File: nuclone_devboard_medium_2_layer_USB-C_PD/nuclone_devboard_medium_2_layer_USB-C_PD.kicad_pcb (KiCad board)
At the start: 2 copper layers, 50 x 76.2 mm, 40 parts, among them J1 JTAG_2X05, J2 TYPE-C-31-M-12, J3 nuclone_medium_left, J4 nuclone_medium_right, J5 Conn_02x06_Odd_Even, SW1 RESET, SW2 Bootloader, U1 MCP1702-3.3V, U2 TPESD0504C6

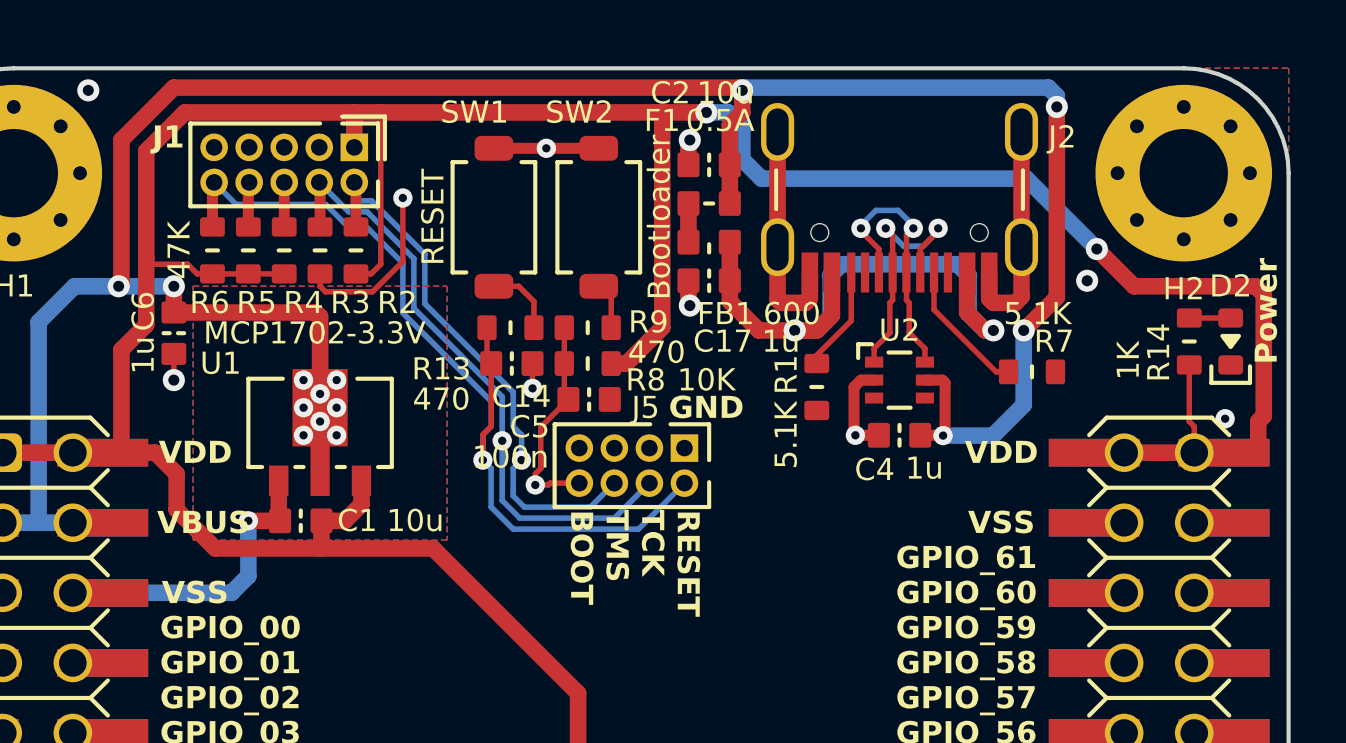
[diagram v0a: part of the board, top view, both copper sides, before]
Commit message: completed medium nuclone with USB-C PD connector
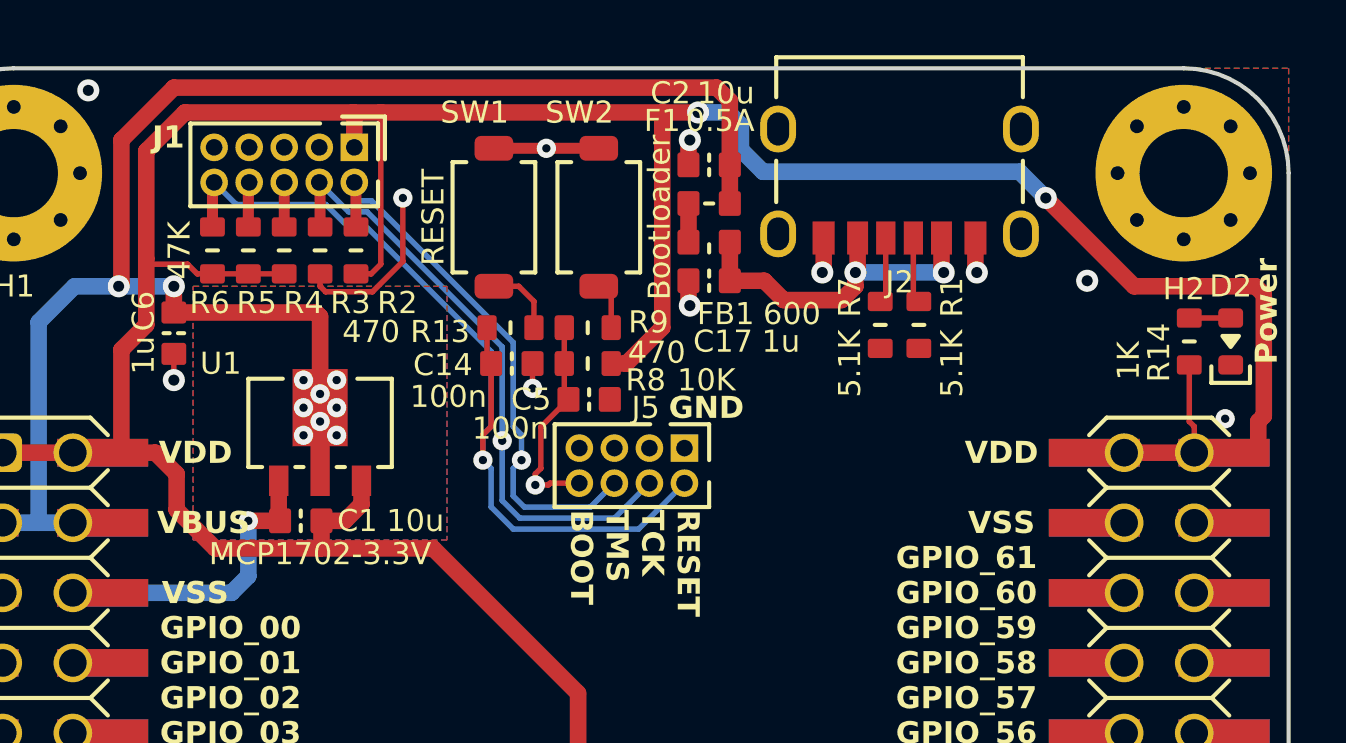
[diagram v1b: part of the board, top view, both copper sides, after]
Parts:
- removed C4: 1u, SquantorCapacitor:C_0603
- removed U2: TPESD0504C6, SquantorIC:SOT363-ONsemi
- J2: footprint SquantorUsb:USB-C-HRO-31-M-12_aisler -> SquantorUsb:USB-C-HRO-31-M-17_aisler
- N2: value V20240114 -> V20240124
- N5: value Nuclone Template V20240114 -> Nuclone Template V20240124
- moved R7 5.76 mm to (95.3, 70.3), turned to 90 degrees
- moved R1 4.33 mm to (96.7, 70.3)
- moved J2 1.25 mm to (96.0, 67.2)
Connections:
- C17 pad 2: Net-(C17-Pad2) -> /VUSB
- FB1 pad 2: Net-(C17-Pad2) -> /VUSB
- R1 pad 2: Net-(J2-CC2) -> Net-(J2-CC1)
- R7 pad 2: Net-(J2-CC1) -> Net-(J2-CC2)
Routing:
- net /VBUS: track 91.2 -> 60.2 mm, vias 14 -> 10
- net Net-(C17-Pad2): track 21.6 -> 0.00 mm, vias 2 -> 0
- net /VSS: track 44.6 -> 27.2 mm, vias 13 -> 14
- net /VUSB: track 0.00 -> 12.7 mm, vias 0 -> 2
- net /DP: track 10.4 -> 0.00 mm, vias 2 -> 0
- net /DN: track 9.60 -> 0.00 mm, vias 2 -> 0
- net Net-(J2-CC1): track 4.98 -> 2.38 mm
- net Net-(J2-CC2): track 3.89 -> 2.38 mm

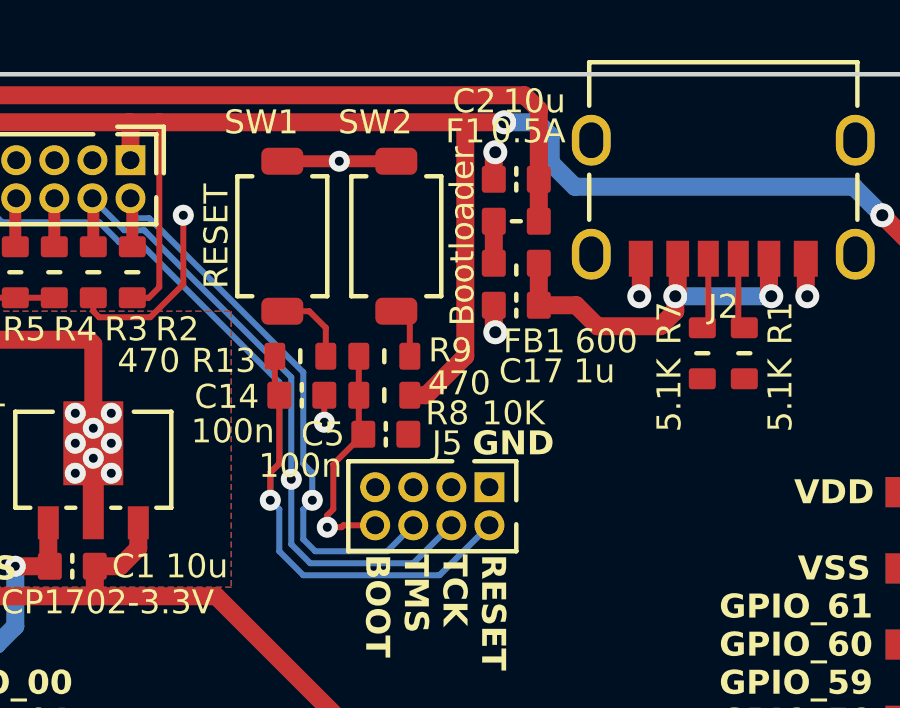
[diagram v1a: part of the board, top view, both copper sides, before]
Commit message: added diode in USB power line
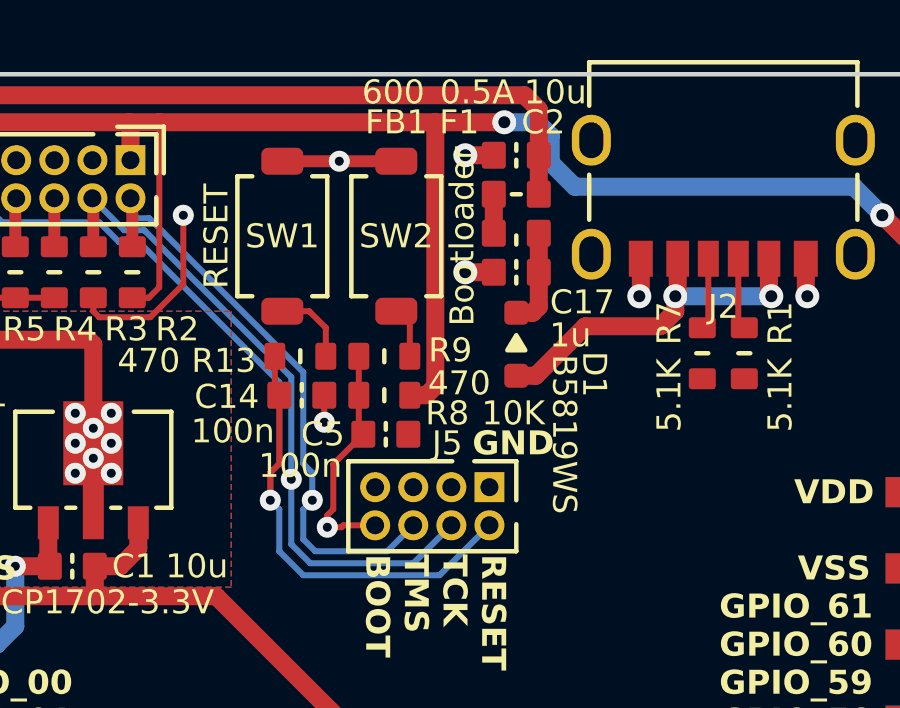
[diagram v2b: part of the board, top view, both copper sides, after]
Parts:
- added D1: B5819WS, SquantorDiodes:SOD-323-nexperia-hand, F.Cu at (89.1, 70.0)
- moved C17 1.10 mm to (89.1, 67.6)
- moved FB1 1.00 mm to (89.1, 66.3)
- moved F1 0.90 mm to (89.1, 65.0)
- moved C2 0.80 mm to (89.1, 63.7)
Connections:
- C17 pad 2: /VUSB -> Net-(D1-K)
- FB1 pad 2: /VUSB -> Net-(D1-K)
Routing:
- net Net-(D1-K): track 0.00 -> 3.28 mm
- net /VBUS: track 60.2 -> 59.3 mm

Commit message: small updates and positioning
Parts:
- moved N2 43.2 mm to (54.8, 103.0)
- moved N1 43.2 mm to (54.9, 99.0)
- moved N3 43.2 mm to (54.8, 104.6)
- moved N4 43.2 mm to (54.8, 104.8)
- moved R1 43.2 mm to (66.6, 39.3)
- moved R13 43.2 mm to (51.8, 39.4)
- moved R9 43.2 mm to (54.6, 39.4)
- moved C1 43.2 mm to (44.2, 46.4)
- moved C14 43.2 mm to (51.9, 40.7)
- moved C2 43.2 mm to (59.0, 32.7)
- moved C3 43.2 mm to (55.0, 60.0)
- moved C5 43.2 mm to (54.6, 42.0)
- moved D1 43.2 mm to (59.0, 39.0)
- moved D2 43.2 mm to (77.9, 39.9)
- moved F1 43.2 mm to (59.0, 34.0)
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
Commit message: updated boards
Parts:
- N2: value V20240124 -> V20240606
- N4: value NuClone Medium template V1.3 -> NuClone Medium template V1.5.1
- N5: value Nuclone Template V20240124 -> Nuclone Template V20240606
- moved C3 8.10 mm to (55.0, 68.1)
- moved C17 0.30 mm to (59.0, 36.9)
- moved D1 0.30 mm to (59.0, 39.3)
- moved H2 0.28 mm to (76.4, 33.6)
- moved H1 0.28 mm to (33.6, 33.6)
- moved H3 0.28 mm to (76.4, 102.6)
- moved H4 0.28 mm to (33.6, 102.6)
- moved FB1 0.20 mm to (59.0, 35.5)
- moved J5 0.20 mm to (56.2, 44.6)
- moved F1 0.10 mm to (59.0, 34.1)
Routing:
- net /VDD: track 128.1 -> 136.2 mm
- net /VSS: track 27.2 -> 34.8 mm
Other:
- outline, holes or cut-outs redrawn

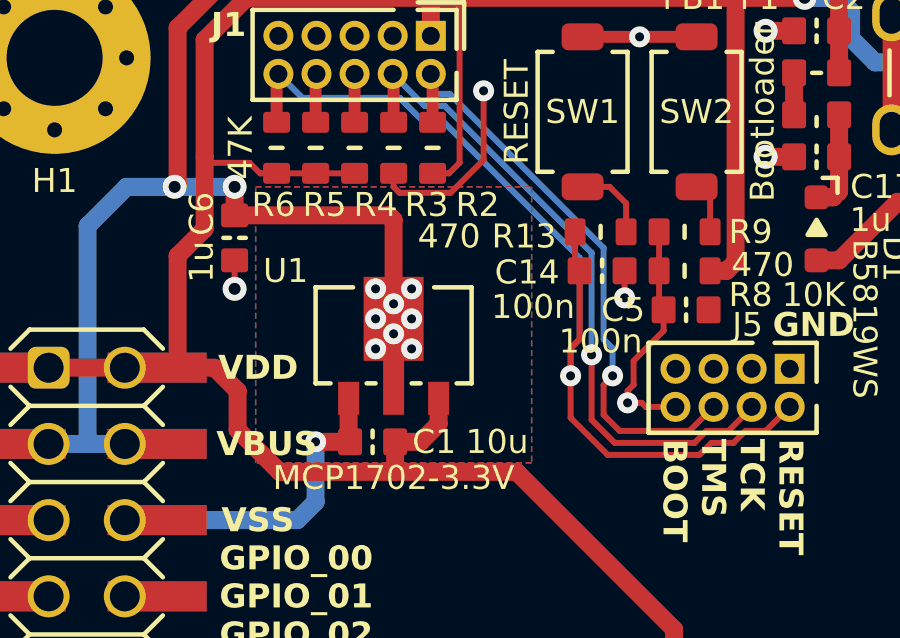
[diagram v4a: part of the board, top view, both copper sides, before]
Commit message: updated silkscreen
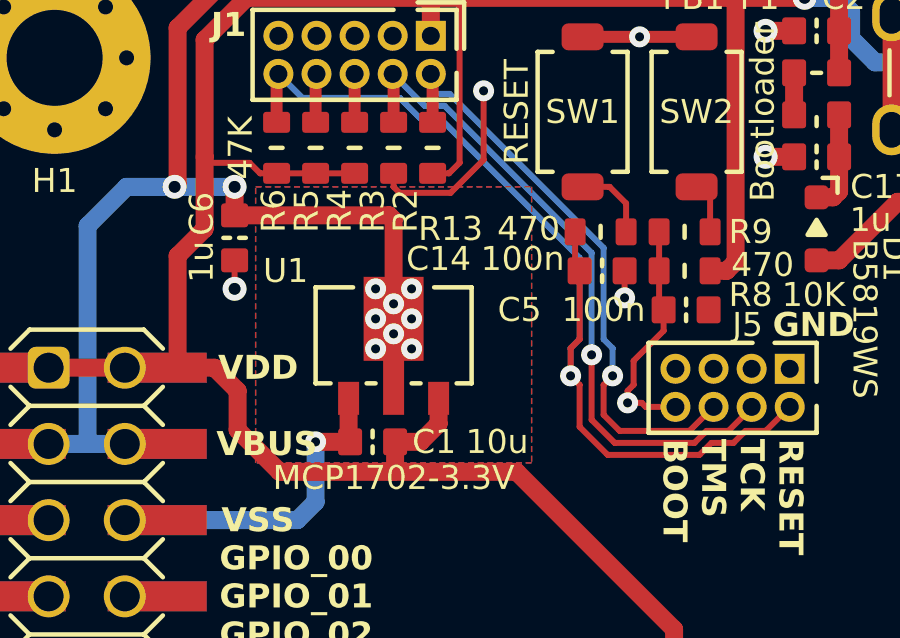
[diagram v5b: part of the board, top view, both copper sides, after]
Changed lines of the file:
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@@
     (property "ki_keywords" "R res resistor")
     (attr smd)
-    (fp_text reference "R3" (at 1.9 -1.1) (layer "F.SilkS")
+    (fp_text reference "R3" (at 2.1 0.7 90) (layer "F.SilkS")
         (effects (font (size 0.8 0.8) (thickness 0.15)))
     )
@@
     (property "ki_keywords" "R res resistor")
     (attr smd)
-    (fp_text reference "R5" (at 1.9 -0.3) (layer "F.SilkS")
+    (fp_text reference "R5" (at 2.1 0.3 90) (layer "F.SilkS")
         (effects (font (size 0.8 0.8) (thickness 0.15)))
     )
@@
     (property "ki_keywords" "R res resistor")
     (attr smd)
-    (fp_text reference "R6" (at 1.9 0.1) (layer "F.SilkS")
+    (fp_text reference "R6" (at 2.1 0.1 90) (layer "F.SilkS")
         (effects (font (size 0.8 0.8) (thickness 0.15)))
     )
@@
     (property "ki_keywords" "cap capacitor")
     (attr smd)
-    (fp_text reference "C14" (at 2.5 -0.05) (layer "F.SilkS")
+    (fp_text reference "C14" (at 5.45 0.4) (layer "F.SilkS")
         (effects (font (size 0.8 0.8) (thickness 0.15)))
     )
-    (fp_text value "100n" (at 2.3 -1.2) (layer "F.SilkS")
+    (fp_text value "100n" (at 2.65 0.4) (layer "F.SilkS")
         (effects (font (size 0.8 0.8) (thickness 0.15)))
     )
@@
     (property "ki_keywords" "R res resistor")
     (attr smd)
-    (fp_text reference "R13" (at -2.55 0.15) (layer "F.SilkS")
+    (fp_text reference "R13" (at -5 -0.1) (layer "F.SilkS")
         (effects (font (size 0.8 0.8) (thickness 0.15)))
     )
-    (fp_text value "470" (at -5.05 0.15) (layer "F.SilkS")
+    (fp_text value "470" (at -2.4 -0.1) (layer "F.SilkS")
         (effects (font (size 0.8 0.8) (thickness 0.15)))
     )
@@
     (property "ki_keywords" "R res resistor")
     (attr smd)
-    (fp_text reference "R2" (at 1.9 -1.5) (layer "F.SilkS")
+    (fp_text reference "R2" (at 2.1 0.9 90) (layer "F.SilkS")
         (effects (font (size 0.8 0.8) (thickness 0.15)))
     )
@@
     (property "ki_keywords" "R res resistor")
     (attr smd)
-    (fp_text reference "R4" (at 1.9 -0.7) (layer "F.SilkS")
+    (fp_text reference "R4" (at 2.1 0.5 90) (layer "F.SilkS")
         (effects (font (size 0.8 0.8) (thickness 0.15)))
     )
@@
     (property "ki_keywords" "cap capacitor")
     (attr smd)
-    (fp_text reference "C5" (at -2.1 0) (layer "F.SilkS")
+    (fp_text reference "C5" (at -5.55 0) (layer "F.SilkS")
         (effects (font (size 0.8 0.8) (thickness 0.15)))
     )
-    (fp_text value "100n" (at -2.85 1.05) (layer "F.SilkS")
+    (fp_text value "100n" (at -2.75 0) (layer "F.SilkS")
         (effects (font (size 0.8 0.8) (thickness 0.15)))
     )
@@
   (segment (start 42.3 34.165) (end 42.33 34.135) (width 0.4) (layer "F.Cu") (net 17))
   (segment (start 42.3 35.75) (end 42.3 34.165) (width 0.4) (layer "F.Cu") (net 17))
+  (segment (start 55.496372 46.435) (end 55.096371 46.835) (width 0.2) (layer "F.Cu") (net 18))
   (segment (start 51.1 42.980761) (end 51.1 40.7) (width 0.2) (layer "F.Cu") (net 18))
-  (segment (start 50.8 45.6) (end 50.8 44.2) (width 0.2) (layer "F.Cu") (net 18))
-  (segment (start 52.035 46.835) (end 50.8 45.6) (width 0.2) (layer "F.Cu") (net 18))
-  (segment (start 56.230685 46.435) (end 55.496372 46.435) (width 0.2) (layer "F.Cu") (net 18))
+  (segment (start 52.035 46.835) (end 51.1 45.9) (width 0.2) (layer "F.Cu") (net 18))
   (segment (start 41 35.75) (end 41 34.195) (width 0.4) (layer "F.Cu") (net 18))
   (segment (start 50.95 39.4) (end 50.95 40.55) (width 0.2) (layer "F.Cu") (net 18))
+  (segment (start 51.1 44.5) (end 50.8 44.2) (width 0.2) (layer "F.Cu") (net 18))
+  (segment (start 56.230685 46.435) (end 55.496372 46.435) (width 0.2) (layer "F.Cu") (net 18))
   (segment (start 50.8 43.280761) (end 51.1 42.980761) (width 0.2) (layer "F.Cu") (net 18))
-  (segment (start 55.096371 46.835) (end 52.035 46.835) (width 0.2) (layer "F.Cu") (net 18))
   (segment (start 41 34.195) (end 41.06 34.135) (width 0.4) (layer "F.Cu") (net 18))
-  (segment (start 58.105 45.235) (end 57.305 46.035) (width 0.2) (layer "F.Cu") (net 18))
   (segment (start 50.95 40.55) (end 51.1 40.7) (width 0.2) (layer "F.Cu") (net 18))
-  (segment (start 50.8 44.2) (end 50.8 43.280761) (width 0.2) (layer "F.Cu") (net 18))
   (segment (start 57.305 46.035) (end 56.630686 46.035) (width 0.2) (layer "F.Cu") (net 18))
-  (segment (start 55.496372 46.435) (end 55.096371 46.835) (width 0.2) (layer "F.Cu") (net 18))
+  (segment (start 51.1 45.9) (end 51.1 44.5) (width 0.2) (layer "F.Cu") (net 18))
+  (segment (start 55.096371 46.835) (end 52.035 46.835) (width 0.2) (layer "F.Cu") (net 18))
+  (segment (start 50.8 44.2) (end 50.8 43.280761) (width 0.2) (layer "F.Cu") (net 18))
+  (segment (start 58.105 45.235) (end 57.305 46.035) (width 0.2) (layer "F.Cu") (net 18))
   (segment (start 56.630686 46.035) (end 56.230685 46.435) (width 0.2) (layer "F.Cu") (net 18))
   (via (at 50.8 44.2) (size 0.7) (drill 0.3) (layers "F.Cu" "B.Cu") (net 18))
